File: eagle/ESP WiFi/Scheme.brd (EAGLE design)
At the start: 160 x 100.3 mm, 8 parts

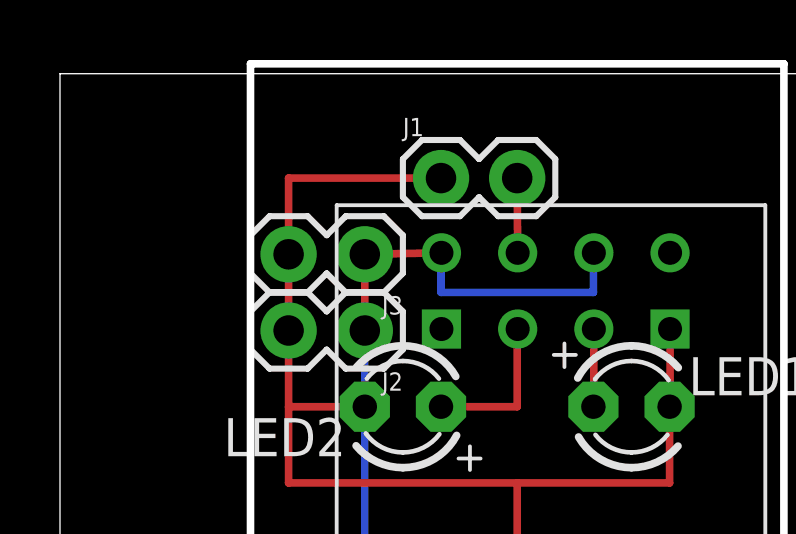
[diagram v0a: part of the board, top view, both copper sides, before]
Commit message: moved LAMP config to .VARIANT
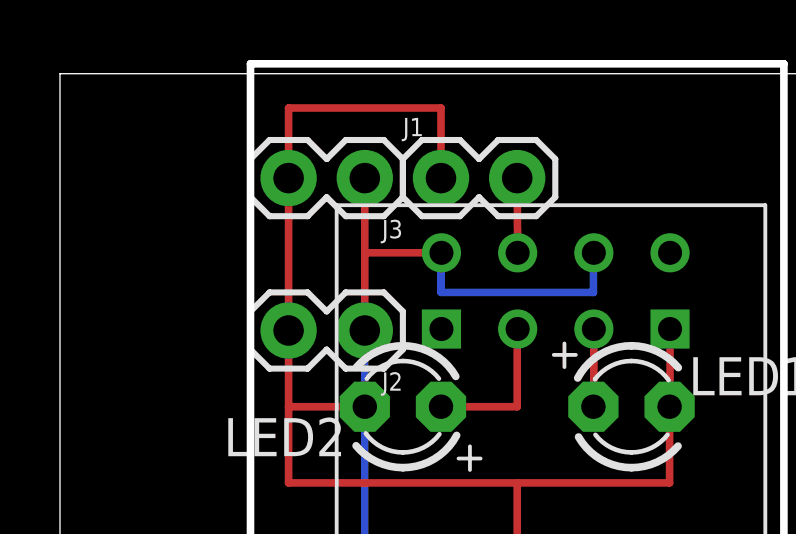
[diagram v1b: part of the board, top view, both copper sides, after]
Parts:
- moved J3 2.54 mm to (10.2, 96.5)
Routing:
- net GND: track 53.4 -> 58.1 mm
- net VCC: track 25.4 -> 28.0 mm
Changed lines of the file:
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@@
 <layer number="21" name="tPlace" color="7" fill="1" visible="yes" active="yes"/>
 <layer number="22" name="bPlace" color="7" fill="1" visible="yes" active="yes"/>
-<layer number="23" name="tOrigins" color="15" fill="1" visible="no" active="yes"/>
-<layer number="24" name="bOrigins" color="15" fill="1" visible="no" active="yes"/>
+<layer number="23" name="tOrigins" color="15" fill="1" visible="yes" active="yes"/>
+<layer number="24" name="bOrigins" color="15" fill="1" visible="yes" active="yes"/>
 <layer number="25" name="tNames" color="7" fill="1" visible="no" active="yes"/>
 <layer number="26" name="bNames" color="7" fill="1" visible="no" active="yes"/>
@@
 <element name="J1" library="SparkFun-Connectors" library_urn="urn:adsk.eagle:library:513" package="1X02" package3d_urn="urn:adsk.eagle:package:38039/1" value="" x="12.7" y="96.52"/>
 <element name="J2" library="SparkFun-Connectors" library_urn="urn:adsk.eagle:library:513" package="1X02" package3d_urn="urn:adsk.eagle:package:38039/1" value="" x="10.16" y="91.44" rot="R180"/>
-<element name="J3" library="SparkFun-Connectors" library_urn="urn:adsk.eagle:library:513" package="1X02" package3d_urn="urn:adsk.eagle:package:38039/1" value="" x="10.16" y="93.98" rot="R180"/>
+<element name="J3" library="SparkFun-Connectors" library_urn="urn:adsk.eagle:library:513" package="1X02" package3d_urn="urn:adsk.eagle:package:38039/1" value="" x="10.16" y="96.52" rot="R180"/>
 <element name="LED1" library="adafruit" library_urn="urn:adsk.eagle:library:420" package="LED3MM" value="" x="19.05" y="88.9"/>
 <element name="LED2" library="adafruit" library_urn="urn:adsk.eagle:library:420" package="LED3MM" value="" x="11.43" y="88.9" rot="R180"/>
@@
 <wire x1="20.335" y1="88.915" x2="20.335" y2="91.4895" width="0.254" layer="1"/>
 <wire x1="20.32" y1="88.9" x2="20.335" y2="88.915" width="0.254" layer="1"/>
-<wire x1="12.7" y1="96.52" x2="7.62" y2="96.52" width="0.254" layer="1"/>
-<wire x1="7.62" y1="93.98" x2="7.62" y2="96.52" width="0.254" layer="1"/>
 <wire x1="7.62" y1="88.9" x2="7.62" y2="91.44" width="0.254" layer="1"/>
 <wire x1="7.62" y1="88.9" x2="7.62" y2="86.36" width="0.254" layer="1"/>
@@
 <wire x1="20.32" y1="86.36" x2="20.32" y2="88.9" width="0.254" layer="1"/>
 <wire x1="10.16" y1="88.9" x2="7.62" y2="88.9" width="0.254" layer="1"/>
-<wire x1="7.62" y1="91.44" x2="7.62" y2="93.98" width="0.254" layer="1"/>
+<wire x1="7.62" y1="91.44" x2="7.62" y2="96.52" width="0.254" layer="1"/>
 <wire x1="15.24" y1="78.74" x2="15.24" y2="86.36" width="0.254" layer="1"/>
 <wire x1="12.7" y1="71.12" x2="15.24" y2="71.12" width="0.254" layer="1"/>
 <wire x1="15.24" y1="71.12" x2="15.24" y2="78.74" width="0.254" layer="1"/>
+<wire x1="7.62" y1="96.52" x2="7.62" y2="98.857" width="0.254" layer="1"/>
+<wire x1="7.62" y1="98.857" x2="12.7" y2="98.857" width="0.254" layer="1"/>
+<wire x1="12.7" y1="98.857" x2="12.7" y2="96.52" width="0.254" layer="1"/>
 </signal>
 <signal name="VCC">
@@
 <contactref element="C1" pad="1"/>
 <wire x1="10.16" y1="93.98" x2="10.16" y2="91.44" width="0.254" layer="1"/>
-<wire x1="12.715" y1="94.0295" x2="10.16" y2="93.98" width="0.254" layer="1"/>
+<wire x1="10.16" y1="93.98" x2="10.16" y2="96.52" width="0.254" layer="1"/>
 <wire x1="10.16" y1="91.44" x2="10.16" y2="78.74" width="0.254" layer="16"/>
 <wire x1="10.16" y1="78.74" x2="10.16" y2="71.12" width="0.254" layer="1"/>
+<wire x1="12.7" y1="94.0445" x2="12.715" y2="94.0295" width="0.254" layer="1"/>
+<wire x1="12.715" y1="94.0295" x2="10.2095" y2="94.0295" width="0.254" layer="1"/>
+<wire x1="10.2095" y1="94.0295" x2="10.16" y2="93.98" width="0.254" layer="1"/>
 <wire x1="12.715" y1="94.0295" x2="17.795" y2="94.0295" width="0" layer="19" extent="1-1"/>
 </signal>
